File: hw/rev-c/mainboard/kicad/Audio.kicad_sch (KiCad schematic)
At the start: 11 parts, among them J22 AUDIO, U20 LM386

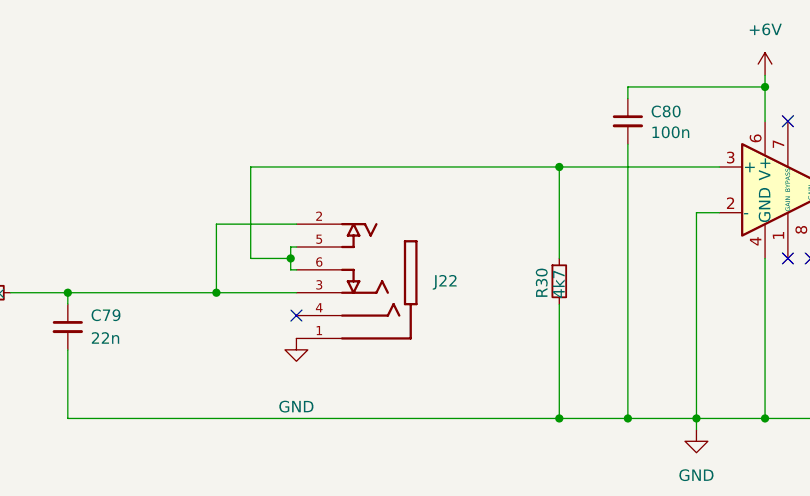
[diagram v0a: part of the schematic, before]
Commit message: hw: fix wire/grid violations in schematic
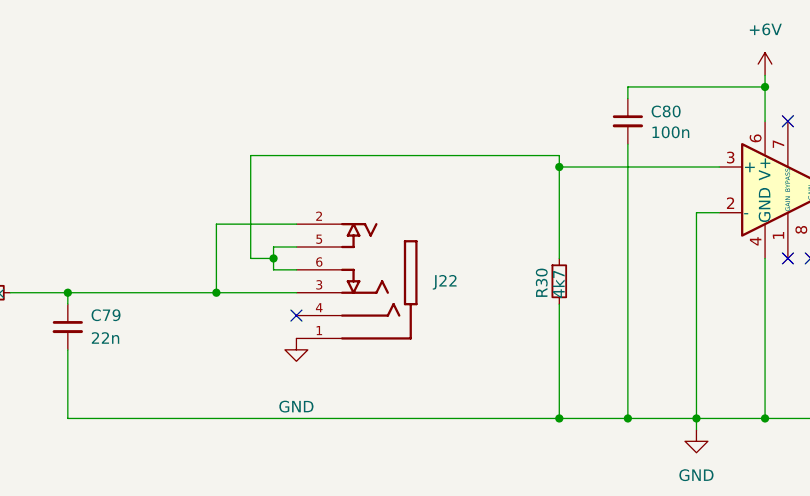
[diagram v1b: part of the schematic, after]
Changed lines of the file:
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@@
+	)
+	(junction
+		(at 110.49 81.28)
+		(diameter 0)
+		(color 0 0 0 0)
 	)
 	(junction
 		(at 181.61 99.06)
-		(diameter 0)
-		(color 0 0 0 0)
-	)
-	(junction
-		(at 112.395 81.28)
 		(diameter 0)
 		(color 0 0 0 0)
@@
 	(wire
 		(pts
-			(xy 112.395 80.01) (xy 113.03 80.01)
-		)
-		(stroke
-			(width 0)
-			(type default)
-		)
-	)
-	(wire
-		(pts
 			(xy 160.02 76.2) (xy 157.48 76.2)
 		)
@@
 	(wire
 		(pts
-			(xy 113.03 82.55) (xy 112.395 82.55)
+			(xy 113.03 82.55) (xy 110.49 82.55)
 		)
 		(stroke
@@
 	(wire
 		(pts
-			(xy 107.95 71.12) (xy 142.24 71.12)
+			(xy 107.95 69.85) (xy 142.24 69.85)
+		)
+		(stroke
+			(width 0)
+			(type default)
+		)
+	)
+	(wire
+		(pts
+			(xy 110.49 80.01) (xy 110.49 81.28)
 		)
 		(stroke
@@
 	(wire
 		(pts
-			(xy 107.95 81.28) (xy 107.95 71.12)
+			(xy 110.49 81.28) (xy 110.49 82.55)
+		)
+		(stroke
+			(width 0)
+			(type default)
+		)
+	)
+	(wire
+		(pts
+			(xy 107.95 81.28) (xy 107.95 69.85)
 		)
 		(stroke
@@
 	(wire
 		(pts
-			(xy 112.395 81.28) (xy 112.395 80.01)
+			(xy 142.24 69.85) (xy 142.24 71.12)
 		)
 		(stroke
@@
 	(wire
 		(pts
-			(xy 112.395 81.28) (xy 107.95 81.28)
+			(xy 107.95 81.28) (xy 110.49 81.28)
 		)
 		(stroke
@@
 	(wire
 		(pts
-			(xy 112.395 82.55) (xy 112.395 81.28)
-		)
-		(stroke
+			(xy 110.49 80.01) (xy 113.03 80.01)
+		)
+		(stroke

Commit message: hw: update transistor and audio jack symbols
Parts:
- J22: symbol SnapEDA:SJ-43504-SMT-TR -> EconoPET:SJ-43504-SMT-TR
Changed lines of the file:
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@@
 	)
 	(symbol
-		(lib_id "SnapEDA:SJ-43504-SMT-TR")
+		(lib_id "EconoPET:SJ-43504-SMT-TR")
 		(at 118.11 85.09 180)
 		(unit 1)

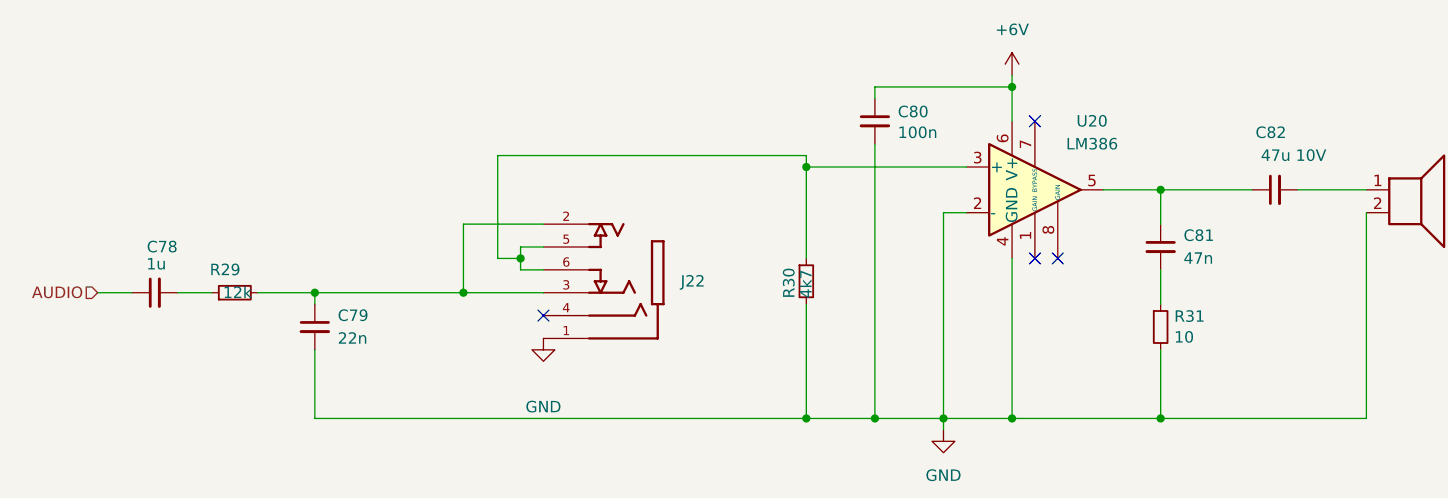
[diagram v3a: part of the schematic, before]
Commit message: hw: renumber reference designators
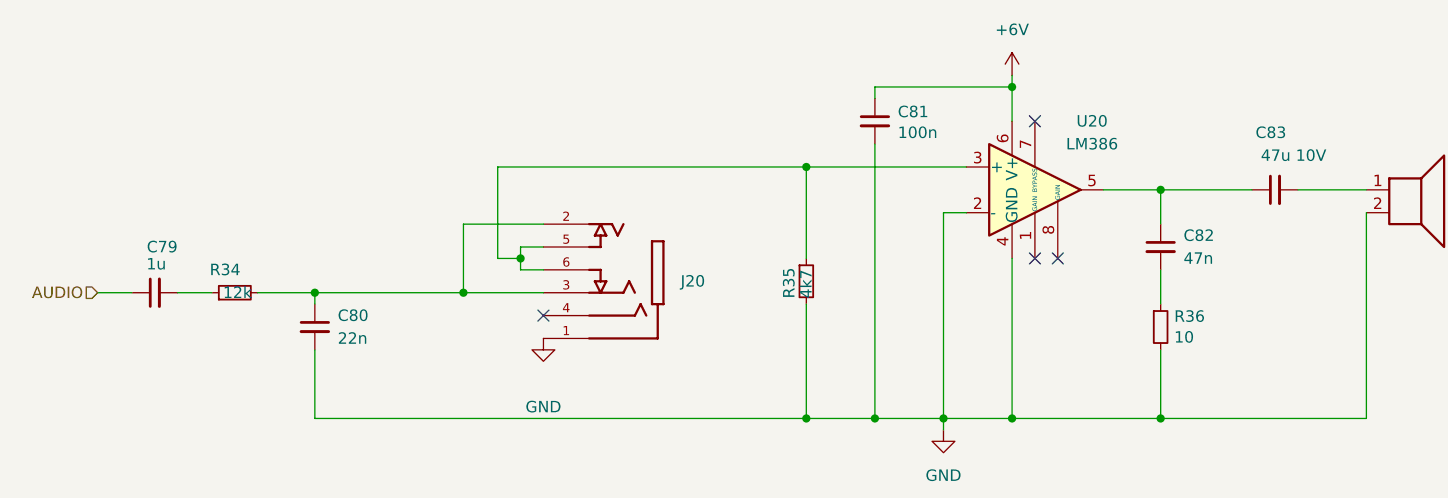
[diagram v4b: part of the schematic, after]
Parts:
- renumbered C78 to C79, C79 to C80, C80 to C81, C81 to C82, C82 to C83, J22 to J20, R29 to R34, R30 to R35, R31 to R36
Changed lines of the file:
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@@
 	(wire
 		(pts
-			(xy 107.95 69.85) (xy 142.24 69.85)
+			(xy 107.95 71.12) (xy 142.24 71.12)
 		)
 		(stroke
@@
 	(wire
 		(pts
-			(xy 107.95 81.28) (xy 107.95 69.85)
+			(xy 107.95 81.28) (xy 107.95 71.12)
 		)
 		(stroke
@@
 		(pts
 			(xy 181.61 99.06) (xy 204.47 99.06)
-		)
-		(stroke
-			(width 0)
-			(type default)
-		)
-	)
-	(wire
-		(pts
-			(xy 142.24 69.85) (xy 142.24 71.12)
 		)
 		(stroke
@@
 		(on_board yes)
 		(dnp no)
-		(property "Reference" "R29"
+		(property "Reference" "R34"
 			(at 79.375 82.55 90)
 			(effects
@@
 			(project ""
 				(path "/2eea20e6-112c-411a-b615-885ae773135a/5178399f-3ceb-4969-8efa-17e54018f3f1"
-					(reference "R29")
+					(reference "R34")
 					(unit 1)
 				)
@@
 		(on_board yes)
 		(dnp no)
-		(property "Reference" "C80"
+		(property "Reference" "C81"
 			(at 152.4 64.9986 0)
 			(effects
@@
 			(project ""
 				(path "/2eea20e6-112c-411a-b615-885ae773135a/5178399f-3ceb-4969-8efa-17e54018f3f1"
-					(reference "C80")
+					(reference "C81")
 					(unit 1)
 				)
@@
 		(on_board yes)
 		(dnp no)
-		(property "Reference" "#PWR0140"
+		(property "Reference" "#PWR0142"
 			(at 113.03 96.52 0)
 			(effects
@@
 			(project ""
 				(path "/2eea20e6-112c-411a-b615-885ae773135a/5178399f-3ceb-4969-8efa-17e54018f3f1"
-					(reference "#PWR0140")
+					(reference "#PWR0142")
 					(unit 1)
 				)
@@
 		(dnp no)
 		(fields_autoplaced yes)
-		(property "Reference" "#PWR0141"
+		(property "Reference" "#PWR0143"
 			(at 157.48 106.68 0)
 			(effects
@@
 			(project ""
 				(path "/2eea20e6-112c-411a-b615-885ae773135a/5178399f-3ceb-4969-8efa-17e54018f3f1"
-					(reference "#PWR0141")
+					(reference "#PWR0143")
 					(unit 1)
 				)
@@
 		(dnp no)
 		(fields_autoplaced yes)
-		(property "Reference" "#PWR0142"
+		(property "Reference" "#PWR0144"
 			(at 165.1 64.77 0)
 			(effects
@@
 			(project ""
 				(path "/2eea20e6-112c-411a-b615-885ae773135a/5178399f-3ceb-4969-8efa-17e54018f3f1"
-					(reference "#PWR0142")
+					(reference "#PWR0144")
 					(unit 1)
 				)
@@
 		(on_board yes)
 		(dnp no)
-		(property "Reference" "R31"
+		(property "Reference" "R36"
 			(at 183.1086 87.7316 0)
 			(effects
@@
 			(project ""
 				(path "/2eea20e6-112c-411a-b615-885ae773135a/5178399f-3ceb-4969-8efa-17e54018f3f1"
-					(reference "R31")
+					(reference "R36")
 					(unit 1)
 				)
@@
 		(dnp no)
 		(fields_autoplaced yes)
-		(property "Reference" "C79"
+		(property "Reference" "C80"
 			(at 90.17 87.6362 0)
 			(effects
@@
 			(project ""
 				(path "/2eea20e6-112c-411a-b615-885ae773135a/5178399f-3ceb-4969-8efa-17e54018f3f1"
-					(reference "C79")
+					(reference "C80")
 					(unit 1)
 				)
@@
 		(dnp no)
 		(fields_autoplaced yes)
-		(property "Reference" "J22"
+		(property "Reference" "J20"
 			(at 128.27 83.8199 0)
 			(effects
@@
 			(project ""
 				(path "/2eea20e6-112c-411a-b615-885ae773135a/5178399f-3ceb-4969-8efa-17e54018f3f1"
-					(reference "J22")
+					(reference "J20")
 					(unit 1)
 				)
@@
 		(on_board yes)
 		(dnp no)
-		(property "Reference" "R30"
+		(property "Reference" "R35"
 			(at 140.335 85.725 90)
 			(effects
@@
 			(project ""
 				(path "/2eea20e6-112c-411a-b615-885ae773135a/5178399f-3ceb-4969-8efa-17e54018f3f1"
-					(reference "R30")
+					(reference "R35")
 					(unit 1)
 				)
@@
 		(on_board yes)
 		(dnp no)
-		(property "Reference" "C78"
+		(property "Reference" "C79"
 			(at 72.39 80.01 90)
 			(effects
@@
 			(project ""
 				(path "/2eea20e6-112c-411a-b615-885ae773135a/5178399f-3ceb-4969-8efa-17e54018f3f1"
-					(reference "C78")
+					(reference "C79")
 					(unit 1)
 				)
@@
 		(dnp no)
 		(fields_autoplaced yes)
-		(property "Reference" "C81"
+		(property "Reference" "C82"
 			(at 184.15 78.7462 0)
 			(effects
@@
 			(project ""
 				(path "/2eea20e6-112c-411a-b615-885ae773135a/5178399f-3ceb-4969-8efa-17e54018f3f1"
-					(reference "C81")
+					(reference "C82")
 					(unit 1)
 				)
@@
 		(on_board yes)
 		(dnp no)
-		(property "Reference" "C82"
+		(property "Reference" "C83"
 			(at 195.58 67.31 90)
 			(effects
@@
 			(project ""
 				(path "/2eea20e6-112c-411a-b615-885ae773135a/5178399f-3ceb-4969-8efa-17e54018f3f1"
-					(reference "C82")
-					(unit 1)
-				)
+					(reference "C83")
+					(unit 1)
+				)

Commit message: hw: match original PET designators for connectors
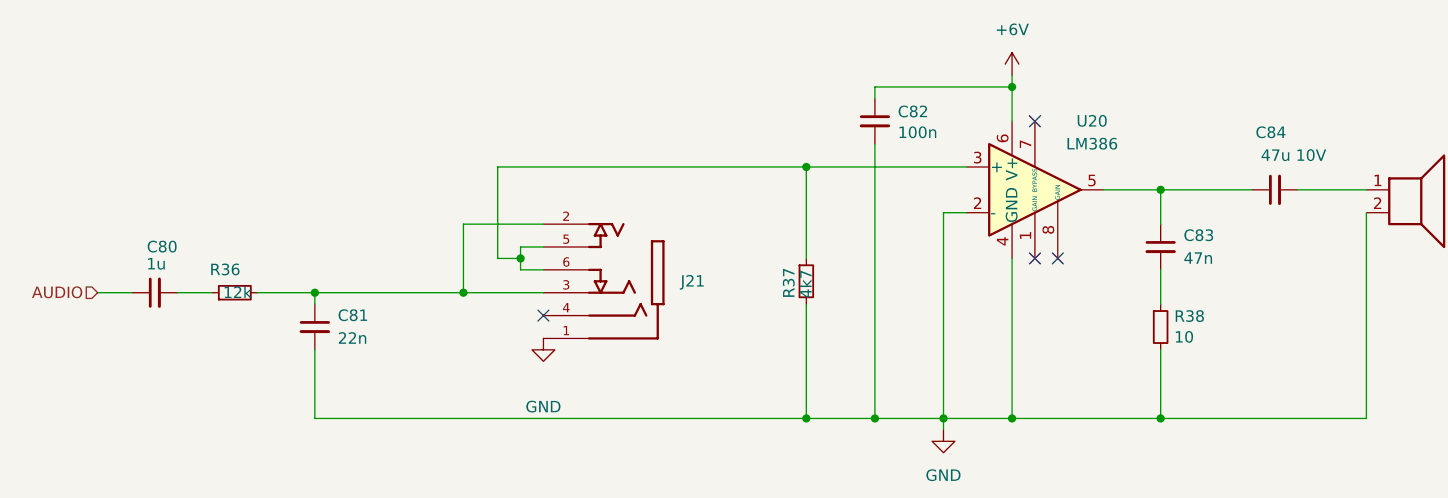
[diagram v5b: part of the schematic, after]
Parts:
- renumbered C79 to C80, C80 to C81, C81 to C82, C82 to C83, C83 to C84, J20 to J21, R34 to R36, R35 to R37, R36 to R38
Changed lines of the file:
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@@
 		(on_board yes)
 		(dnp no)
-		(property "Reference" "R34"
+		(property "Reference" "R36"
 			(at 79.375 82.55 90)
 			(effects
@@
 			(project ""
 				(path "/2eea20e6-112c-411a-b615-885ae773135a/5178399f-3ceb-4969-8efa-17e54018f3f1"
-					(reference "R34")
+					(reference "R36")
 					(unit 1)
 				)
@@
 		(on_board yes)
 		(dnp no)
-		(property "Reference" "C81"
+		(property "Reference" "C82"
 			(at 152.4 64.9986 0)
 			(effects
@@
 			(project ""
 				(path "/2eea20e6-112c-411a-b615-885ae773135a/5178399f-3ceb-4969-8efa-17e54018f3f1"
-					(reference "C81")
+					(reference "C82")
 					(unit 1)
 				)
@@
 		(on_board yes)
 		(dnp no)
-		(property "Reference" "R36"
+		(property "Reference" "R38"
 			(at 183.1086 87.7316 0)
 			(effects
@@
 			(project ""
 				(path "/2eea20e6-112c-411a-b615-885ae773135a/5178399f-3ceb-4969-8efa-17e54018f3f1"
-					(reference "R36")
+					(reference "R38")
 					(unit 1)
 				)
@@
 		(dnp no)
 		(fields_autoplaced yes)
-		(property "Reference" "C80"
+		(property "Reference" "C81"
 			(at 90.17 87.6362 0)
 			(effects
@@
 			(project ""
 				(path "/2eea20e6-112c-411a-b615-885ae773135a/5178399f-3ceb-4969-8efa-17e54018f3f1"
-					(reference "C80")
+					(reference "C81")
 					(unit 1)
 				)
@@
 		(dnp no)
 		(fields_autoplaced yes)
-		(property "Reference" "J20"
+		(property "Reference" "J21"
 			(at 128.27 83.8199 0)
 			(effects
@@
 			(project ""
 				(path "/2eea20e6-112c-411a-b615-885ae773135a/5178399f-3ceb-4969-8efa-17e54018f3f1"
-					(reference "J20")
+					(reference "J21")
 					(unit 1)
 				)
@@
 		(on_board yes)
 		(dnp no)
-		(property "Reference" "R35"
+		(property "Reference" "R37"
 			(at 140.335 85.725 90)
 			(effects
@@
 			(project ""
 				(path "/2eea20e6-112c-411a-b615-885ae773135a/5178399f-3ceb-4969-8efa-17e54018f3f1"
-					(reference "R35")
+					(reference "R37")
 					(unit 1)
 				)
@@
 		(on_board yes)
 		(dnp no)
-		(property "Reference" "C79"
+		(property "Reference" "C80"
 			(at 72.39 80.01 90)
 			(effects
@@
 			(project ""
 				(path "/2eea20e6-112c-411a-b615-885ae773135a/5178399f-3ceb-4969-8efa-17e54018f3f1"
-					(reference "C79")
+					(reference "C80")
 					(unit 1)
 				)
@@
 		(dnp no)
 		(fields_autoplaced yes)
-		(property "Reference" "C82"
+		(property "Reference" "C83"
 			(at 184.15 78.7462 0)
 			(effects
@@
 			(project ""
 				(path "/2eea20e6-112c-411a-b615-885ae773135a/5178399f-3ceb-4969-8efa-17e54018f3f1"
-					(reference "C82")
+					(reference "C83")
 					(unit 1)
 				)
@@
 		(on_board yes)
 		(dnp no)
-		(property "Reference" "C83"
+		(property "Reference" "C84"
 			(at 195.58 67.31 90)
 			(effects
@@
 			(project ""
 				(path "/2eea20e6-112c-411a-b615-885ae773135a/5178399f-3ceb-4969-8efa-17e54018f3f1"
-					(reference "C83")
-					(unit 1)
-				)
+					(reference "C84")
+					(unit 1)
+				)

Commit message: hw: move speaker to EconoPET library
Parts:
- LS1: footprint SamacSys_Parts:AT1220TT9R -> EconoPET:AT1220TT9R
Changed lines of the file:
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@@
 			)
 		)
-		(property "Footprint" "SamacSys_Parts:AT1220TT9R"
+		(property "Footprint" "EconoPET:AT1220TT9R"
 			(at 209.55 78.74 0)
 			(effects

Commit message: hw: bjt audio
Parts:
- removed R38: 10, Resistor_SMD:R_0805_2012Metric_Pad1.20x1.40mm_HandSolder, symbol Device:R_Small
- removed U20: LM386, Package_DIP:DIP-8_W7.62mm, symbol Amplifier_Audio:LM386
- added C105: 47n, Capacitor_SMD:C_0603_1608Metric, symbol Device:C_Small
- added C106, C107: 100n, Capacitor_SMD:C_0402_1005Metric, symbol Device:C_Small
- added C8: 47u 10V, Capacitor_SMD:C_1206_3216Metric, symbol Device:C_Small
- added D13, D14: 1N4148WS, Diode_SMD:D_SOD-323, symbol Simulation_SPICE:D
- added Q4, Q5, Q6: SS8050, Package_TO_SOT_SMD:SOT-23, symbol Transistor_BJT:SS8050
- added Q7: SS8550, Package_TO_SOT_SMD:SOT-23, symbol Transistor_BJT:SS8550
- added R67, R69: 1k5, Resistor_SMD:R_0402_1005Metric, symbol Device:R_Small
- added R68: 680, Resistor_SMD:R_0402_1005Metric, symbol Device:R_Small
- added R70: 10k, Resistor_SMD:R_0402_1005Metric, symbol Device:R_Small
- added R71: 100k, Resistor_SMD:R_0402_1005Metric, symbol Device:R_Small
- added R72, R73: 1, Resistor_SMD:R_0603_1608Metric, symbol Device:R_Small
- added R74: 1k, Resistor_SMD:R_0402_1005Metric, symbol Device:R_Small
- C82: value 100n -> 68n; footprint Capacitor_SMD:C_0402_1005Metric -> Capacitor_SMD:C_0603_1608Metric; LCSC C307331 -> C31658
- C83: value 47n -> 100n; footprint Capacitor_SMD:C_0603_1608Metric -> Capacitor_SMD:C_0402_1005Metric; LCSC C1622 -> C307331
- LS1: value Speaker -> 42Ω SPK
- R36: footprint Resistor_SMD:R_0805_2012Metric_Pad1.20x1.40mm_HandSolder -> Resistor_SMD:R_0402_1005Metric; LCSC C17444 -> C25752
- R37: value 4k7 -> 22k; footprint Resistor_SMD:R_0805_2012Metric_Pad1.20x1.40mm_HandSolder -> Resistor_SMD:R_0402_1005Metric; LCSC C17673 -> C25768
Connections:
- net +6V: now also C106.1, C107.1, Q6.3 (C), R70.1, R74.1; no longer C82.1
- net GND: now also C83.2, C106.2, C107.2, Q4.2 (E), Q5.2 (E), Q7.3 (C), R68.1; no longer C82.2, R37.2
- net at J21.5, J21.6, R37.1: now also Q4.1 (B)
- net at C84.2, LS1.1: now also C8.2
- net at C83.1: now also R67.2, R69.1; no longer C84.1
- new net: D13.1 (K), D14.2 (A)
- new net: D13.2 (A), Q6.1 (B), R74.2
- new net: C82.1, Q4.3 (C), R37.2, R67.1, R70.2
- new net: Q6.2 (E), R72.1
- new net: C8.1, C84.1, R71.1, R72.2, R73.1
- new net: C105.1, Q5.1 (B), R69.2, R71.2
- new net: C105.2, C82.2, R68.2
- new net: D14.1 (K), Q5.3 (C), Q7.1 (B)
- new net: Q7.2 (E), R73.2
- no-connect marks 4 -> 1
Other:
- note added: "The AUDIO source is ΔΣ encoded 1-bit output from the FPGA (3.3V at 64 MHz). The 1u capacitor and 12k resistor adjusts this to line-level audio, which is +/- 0.5V AC for consumer electronics. (Note that the amplifiers and powered speakers typically provide a 10k resistor to ground to form a voltage divider.)"
- note added: "Twin-T notch filter compensates for 2 KHz resonant frequency of our chosen speaker."
- note removed: "The AUDIO source is the ΔΣ encoded 1-bit output from the FPGA (3.3V), not the CB2 signal from the VIA. This gives the FPGA the opportunity to filter the audio and/or mix additional sources, such as an FPGA emulated SID. (See PETSID: http://www.cbmhardware.de/show.php?r=14&id=71/PETSID) The FPGA to implements the NAND gate between CB2 and DIAG to save an IC. Line-level audio for consumer electroni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"
- moved on the sheet: C80, C81, C84, J21, LS1, R36

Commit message: hw: update 4u7 and silkscreen
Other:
- moved on the sheet: C8, C84
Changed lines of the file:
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@@
 	)
 	(junction
-		(at 217.17 71.12)
+		(at 213.36 71.12)
 		(diameter 0)
 		(color 0 0 0 0)
@@
 	)
 	(junction
-		(at 209.55 71.12)
+		(at 205.74 71.12)
 		(diameter 0)
 		(color 0 0 0 0)
@@
 	(wire
 		(pts
-			(xy 191.77 71.12) (xy 209.55 71.12)
+			(xy 191.77 71.12) (xy 205.74 71.12)
 		)
 		(stroke
@@
 	(wire
 		(pts
-			(xy 209.55 74.93) (xy 210.82 74.93)
+			(xy 205.74 74.93) (xy 207.01 74.93)
 		)
 		(stroke
@@
 	(wire
 		(pts
-			(xy 209.55 74.93) (xy 209.55 71.12)
+			(xy 205.74 74.93) (xy 205.74 71.12)
 		)
 		(stroke
@@
 	(wire
 		(pts
-			(xy 217.17 71.12) (xy 217.17 67.31)
+			(xy 213.36 71.12) (xy 213.36 67.31)
 		)
 		(stroke
@@
 	(wire
 		(pts
-			(xy 217.17 67.31) (xy 215.9 67.31)
+			(xy 213.36 67.31) (xy 212.09 67.31)
 		)
 		(stroke
@@
 	(wire
 		(pts
-			(xy 217.17 74.93) (xy 217.17 71.12)
+			(xy 213.36 74.93) (xy 213.36 71.12)
 		)
 		(stroke
@@
 	(wire
 		(pts
-			(xy 209.55 67.31) (xy 210.82 67.31)
+			(xy 205.74 67.31) (xy 207.01 67.31)
 		)
 		(stroke
@@
 	(wire
 		(pts
-			(xy 217.17 71.12) (xy 220.98 71.12)
+			(xy 213.36 71.12) (xy 220.98 71.12)
 		)
 		(stroke
@@
 	(wire
 		(pts
-			(xy 209.55 71.12) (xy 209.55 67.31)
+			(xy 205.74 71.12) (xy 205.74 67.31)
 		)
 		(stroke
@@
 	(wire
 		(pts
-			(xy 215.9 74.93) (xy 217.17 74.93)
+			(xy 212.09 74.93) (xy 213.36 74.93)
 		)
 		(stroke
@@
 	(symbol
 		(lib_id "Device:C_Small")
-		(at 213.36 67.31 90)
+		(at 209.55 67.31 90)
 		(unit 1)
 		(exclude_from_sim no)
@@
 		(dnp no)
 		(property "Reference" "C8"
-			(at 213.36 60.96 90)
+			(at 209.55 60.96 90)
 			(effects
 				(font
@@
 		)
 		(property "Value" "47u 10V"
-			(at 218.948 63.754 90)
+			(at 215.138 63.754 90)
 			(effects
 				(font
@@
 		)
 		(property "Footprint" "Capacitor_SMD:C_1206_3216Metric"
-			(at 213.36 67.31 0)
+			(at 209.55 67.31 0)
 			(effects
 				(font
@@
 		)
 		(property "Datasheet" "https://product.samsungsem.com/mlcc/CL31A476MPHNNN.do"
-			(at 213.36 67.31 0)
+			(at 209.55 67.31 0)
 			(effects
 				(font
@@
 		)
 		(property "Description" ""
-			(at 213.36 67.31 0)
+			(at 209.55 67.31 0)
 			(effects
 				(font
@@
 		)
 		(property "LCSC" "C96123"
-			(at 213.36 67.31 0)
+			(at 209.55 67.31 0)
 			(effects
 				(font
@@
 	(symbol
 		(lib_id "Device:C_Small")
-		(at 213.36 74.93 90)
+		(at 209.55 74.93 90)
 		(unit 1)
 		(exclude_from_sim no)
@@
 		(dnp no)
 		(property "Reference" "C84"
-			(at 214.63 78.74 90)
+			(at 210.82 78.74 90)
 			(effects
 				(font
@@
 		)
 		(property "Value" "47u 10V"
-			(at 219.075 81.28 90)
+			(at 215.265 81.28 90)
 			(effects
 				(font
@@
 		)
 		(property "Footprint" "Capacitor_SMD:C_1206_3216Metric"
-			(at 213.36 74.93 0)
+			(at 209.55 74.93 0)
 			(effects
 				(font
@@
 		)
 		(property "Datasheet" "https://product.samsungsem.com/mlcc/CL31A476MPHNNN.do"
-			(at 213.36 74.93 0)
+			(at 209.55 74.93 0)
 			(effects
 				(font
@@
 		)
 		(property "Description" ""
-			(at 213.36 74.93 0)
+			(at 209.55 74.93 0)
 			(effects
 				(font
@@
 		)
 		(property "LCSC" "C96123"
-			(at 213.36 74.93 0)
+			(at 209.55 74.93 0)
 			(effects
 				(font
